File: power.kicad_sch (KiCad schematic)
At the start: 28 parts, among them U5 TPS54302, U6 TPS54302

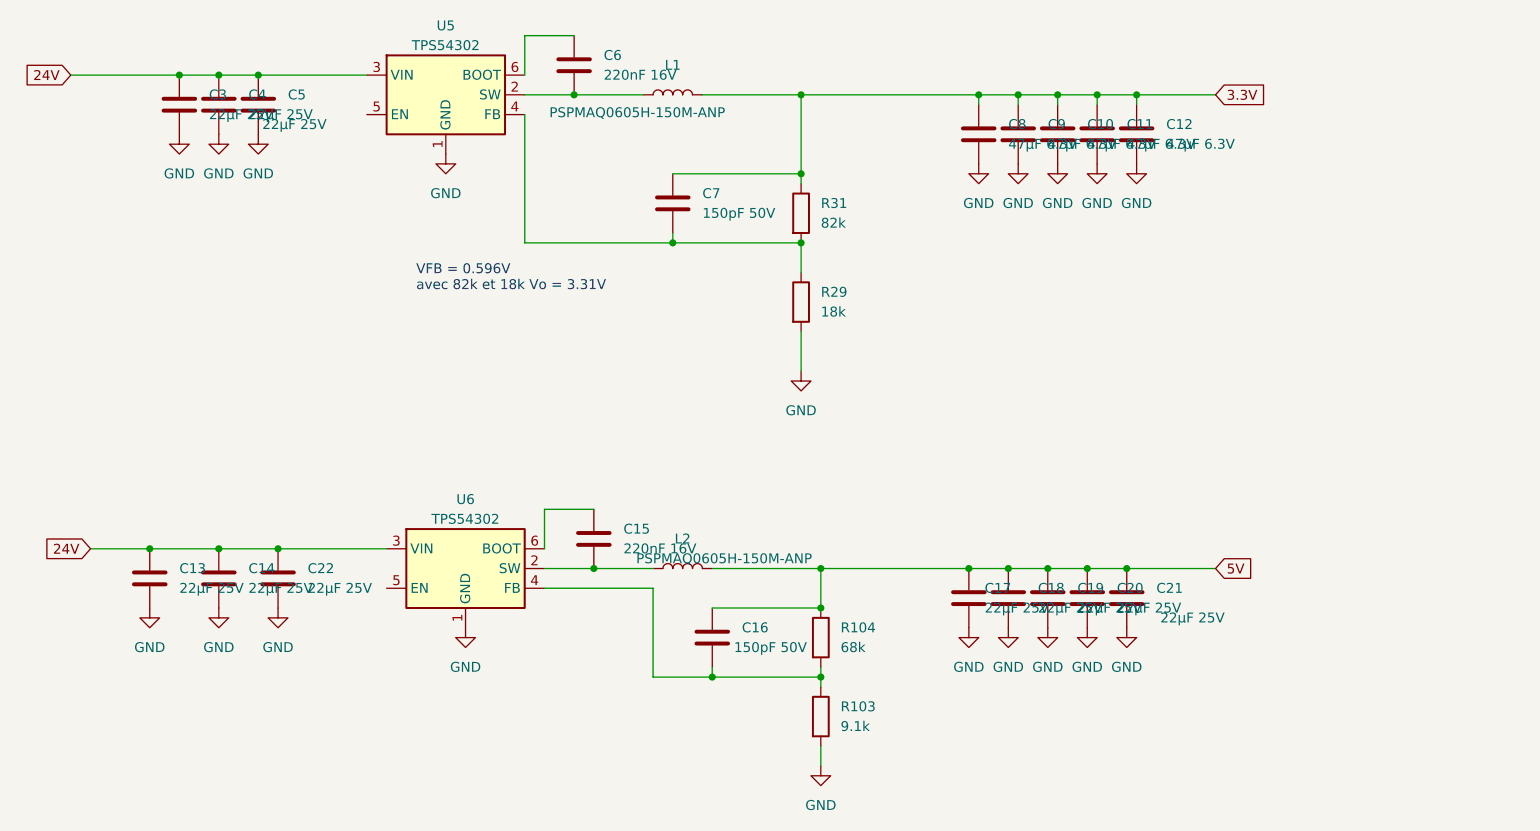
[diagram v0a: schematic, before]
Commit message: update schematic
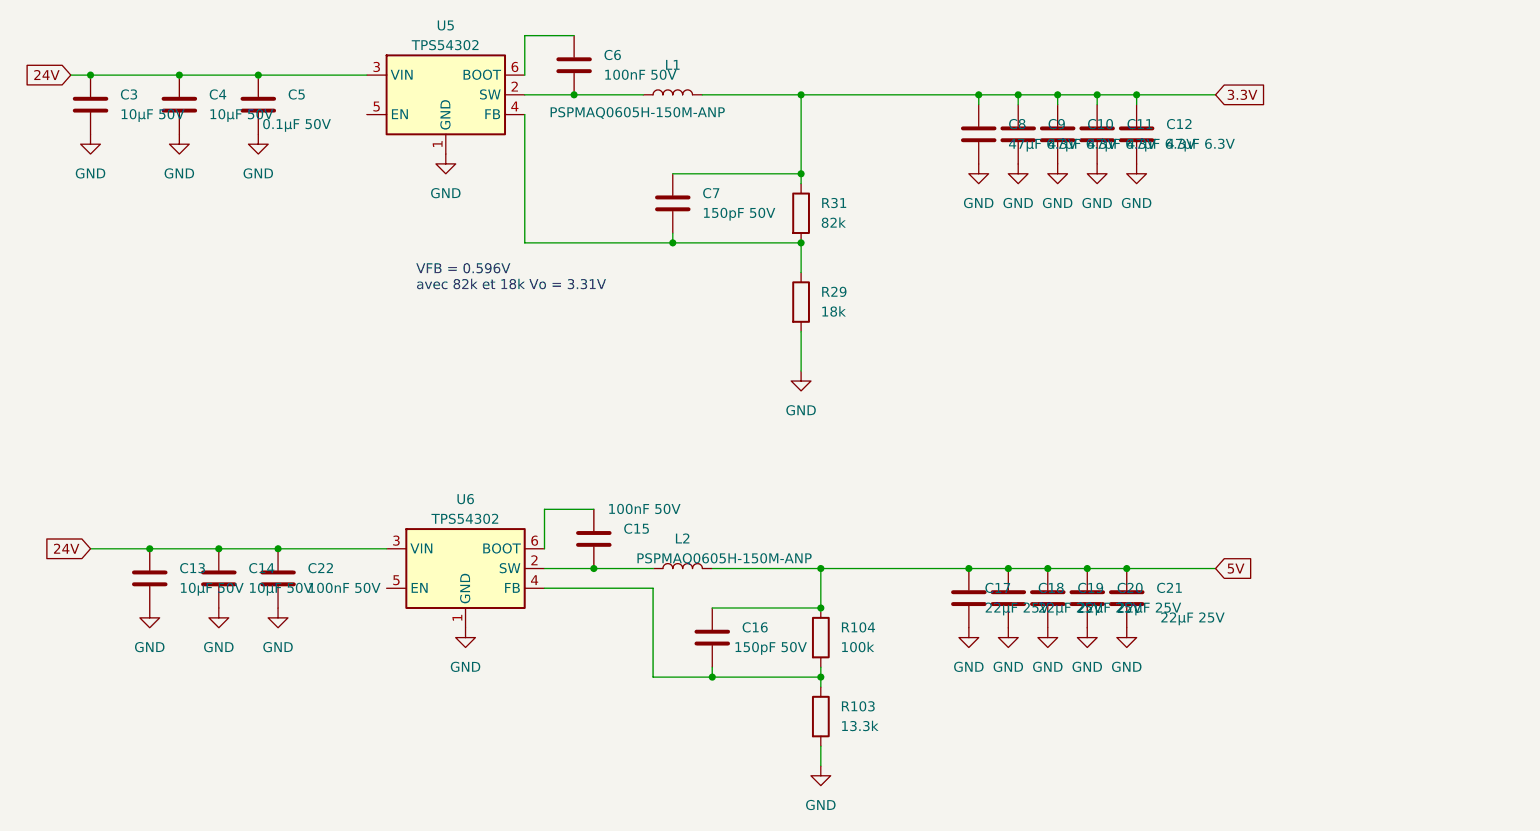
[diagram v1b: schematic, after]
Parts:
- C13, C14, C3, C4: value 22µF 25V -> 10µF 50V
- C15, C6: value 220nF 16V -> 100nF 50V
- C22: value 22µF 25V -> 100nF 50V
- C5: value 22µF 25V -> 0.1µF 50V
- R103: value 9.1k -> 13.3k
- R104: value 68k -> 100k
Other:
- moved on the sheet: C3, C4
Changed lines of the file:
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@@
 	)
 	(junction
+		(at 49.53 27.94)
+		(diameter 0)
+		(color 0 0 0 0)
+	)
+	(junction
 		(at 132.08 105.41)
 		(diameter 0)
@@
 	)
 	(junction
-		(at 54.61 27.94)
-		(diameter 0)
-		(color 0 0 0 0)
-	)
-	(junction
-		(at 49.53 27.94)
+		(at 161.29 91.44)
 		(diameter 0)
 		(color 0 0 0 0)
 	)
 	(junction
-		(at 161.29 91.44)
+		(at 38.1 27.94)
 		(diameter 0)
 		(color 0 0 0 0)
@@
 	(wire
 		(pts
-			(xy 35.56 27.94) (xy 49.53 27.94)
+			(xy 35.56 27.94) (xy 38.1 27.94)
 		)
 		(stroke
@@
 	(wire
 		(pts
-			(xy 49.53 27.94) (xy 54.61 27.94)
+			(xy 54.61 88.9) (xy 62.23 88.9)
 		)
 		(stroke
@@
 	(wire
 		(pts
-			(xy 54.61 88.9) (xy 62.23 88.9)
+			(xy 109.22 30.48) (xy 100.33 30.48)
 		)
 		(stroke
@@
 	(wire
 		(pts
-			(xy 109.22 30.48) (xy 100.33 30.48)
+			(xy 132.08 105.41) (xy 132.08 106.68)
 		)
 		(stroke
@@
 	(wire
 		(pts
-			(xy 132.08 105.41) (xy 132.08 106.68)
+			(xy 38.1 27.94) (xy 49.53 27.94)
 		)
 		(stroke
@@
 	(wire
 		(pts
-			(xy 54.61 27.94) (xy 59.69 27.94)
+			(xy 93.98 27.94) (xy 93.98 22.86)
 		)
 		(stroke
@@
 	(wire
 		(pts
-			(xy 93.98 27.94) (xy 93.98 22.86)
+			(xy 49.53 27.94) (xy 59.69 27.94)
 		)
 		(stroke
@@
 			)
 		)
-		(property "Value" "22µF 25V"
+		(property "Value" "10µF 50V"
 			(at 58.42 93.98 0)
 			(effects
@@
 	(symbol
 		(lib_id "Device:C")
-		(at 49.53 31.75 0)
+		(at 38.1 31.75 0)
 		(unit 1)
 		(exclude_from_sim no)
@@
 		(dnp no)
 		(property "Reference" "C3"
-			(at 53.34 30.48 0)
+			(at 41.91 30.48 0)
 			(effects
 				(font
@@
 			)
 		)
-		(property "Value" "22µF 25V"
-			(at 53.34 33.02 0)
+		(property "Value" "10µF 50V"
+			(at 41.91 33.02 0)
 			(effects
 				(font
@@
 		)
 		(property "Footprint" "Capacitor_SMD:C_0805_2012Metric"
-			(at 50.4952 35.56 0)
+			(at 39.0652 35.56 0)
 			(effects
 				(font
@@
 		)
 		(property "Datasheet" "~"
-			(at 49.53 31.75 0)
+			(at 38.1 31.75 0)
 			(effects
 				(font
@@
 		)
 		(property "Description" ""
-			(at 49.53 31.75 0)
+			(at 38.1 31.75 0)
 			(effects
 				(font
@@
 	(symbol
 		(lib_id "power:GND")
-		(at 49.53 35.56 0)
+		(at 38.1 35.56 0)
 		(unit 1)
 		(exclude_from_sim no)
@@
 		(fields_autoplaced yes)
 		(property "Reference" "#PWR023"
-			(at 49.53 41.91 0)
+			(at 38.1 41.91 0)
 			(effects
 				(font
@@
 		)
 		(property "Value" "GND"
-			(at 49.53 40.64 0)
+			(at 38.1 40.64 0)
 			(effects
 				(font
@@
 		)
 		(property "Footprint" ""
-			(at 49.53 35.56 0)
+			(at 38.1 35.56 0)
 			(effects
 				(font
@@
 		)
 		(property "Datasheet" ""
-			(at 49.53 35.56 0)
+			(at 38.1 35.56 0)
 			(effects
 				(font
@@
 		)
 		(property "Description" ""
-			(at 49.53 35.56 0)
+			(at 38.1 35.56 0)
 			(effects
 				(font
@@
 		(on_board yes)
 		(dnp no)
-		(fields_autoplaced yes)
 		(property "Reference" "C15"
 			(at 106.68 86.36 0)
@@
 			)
 		)
-		(property "Value" "220nF 16V"
-			(at 106.68 88.9 0)
+		(property "Value" "100nF 50V"
+			(at 104.648 83.82 0)
 			(effects
 				(font
@@
 			)
 		)
-		(property "Value" "22µF 25V"
+		(property "Value" "100nF 50V"
 			(at 66.04 93.98 0)
 			(effects
@@
 			)
 		)
-		(property "Value" "68k"
+		(property "Value" "100k"
 			(at 134.62 101.5999 0)
 			(effects
@@
 		(fields_autoplaced yes)
 		(property "Reference" "R103"
-			(at 134.62 109.22 0)
+			(at 134.62 109.2199 0)
 			(effects
 				(font
@@
 			)
 		)
-		(property "Value" "9.1k"
-			(at 134.62 111.76 0)
+		(property "Value" "13.3k"
+			(at 134.62 111.7599 0)
 			(effects
 				(font
@@
 	(symbol
 		(lib_id "power:GND")
-		(at 54.61 35.56 0)
+		(at 49.53 35.56 0)
 		(unit 1)
 		(exclude_from_sim no)
@@
 		(fields_autoplaced yes)
 		(property "Reference" "#PWR025"
-			(at 54.61 41.91 0)
+			(at 49.53 41.91 0)
 			(effects
 				(font
@@
 		)
 		(property "Value" "GND"
-			(at 54.61 40.64 0)
+			(at 49.53 40.64 0)
 			(effects
 				(font
@@
 		)
 		(property "Footprint" ""
-			(at 54.61 35.56 0)
+			(at 49.53 35.56 0)
 			(effects
 				(font
@@
 		)
 		(property "Datasheet" ""
-			(at 54.61 35.56 0)
+			(at 49.53 35.56 0)
 			(effects
 				(font
@@
 		)
 		(property "Description" ""
-			(at 54.61 35.56 0)
+			(at 49.53 35.56 0)
 			(effects
 				(font
@@
 		(fields_autoplaced yes)
 		(property "Reference" "C6"
-			(at 104.14 25.4 0)
+			(at 104.14 25.3999 0)
 			(effects
 				(font
@@
 			)
 		)
-		(property "Value" "220nF 16V"
-			(at 104.14 27.94 0)
+		(property "Value" "100nF 50V"
+			(at 104.14 27.9399 0)
 			(effects
 				(font
@@
 			)
 		)
-		(property "Value" "22µF 25V"
+		(property "Value" "10µF 50V"
 			(at 49.53 93.98 0)
 			(effects
@@
 			)
 		)
-		(property "Value" "22µF 25V"
+		(property "Value" "0.1µF 50V"
 			(at 60.198 34.29 0)
 			(effects
@@
 	(symbol
 		(lib_id "Device:C")
-		(at 54.61 31.75 0)
+		(at 49.53 31.75 0)
 		(unit 1)
 		(exclude_from_sim no)
@@
 		(dnp no)
 		(property "Reference" "C4"
-			(at 58.42 30.48 0)
+			(at 53.34 30.48 0)
 			(effects
 				(font
@@
 			)
 		)
-		(property "Value" "22µF 25V"
-			(at 58.42 33.02 0)
+		(property "Value" "10µF 50V"
+			(at 53.34 33.02 0)
 			(effects
 				(font
@@
 		)
 		(property "Footprint" "Capacitor_SMD:C_0805_2012Metric"
-			(at 55.5752 35.56 0)
+			(at 50.4952 35.56 0)
 			(effects
 				(font
@@
 		)
 		(property "Datasheet" "~"
-			(at 54.61 31.75 0)
+			(at 49.53 31.75 0)
 			(effects
 				(font
@@
 		)
 		(property "Description" ""
-			(at 54.61 31.75 0)
+			(at 49.53 31.75 0)
 			(effects
 				(font

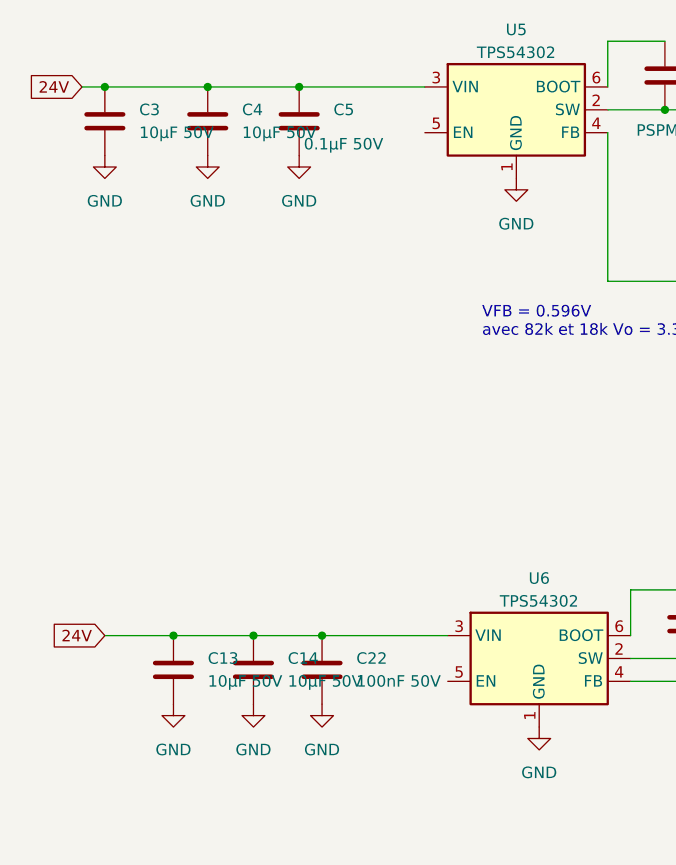
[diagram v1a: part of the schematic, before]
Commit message: update capa footprint
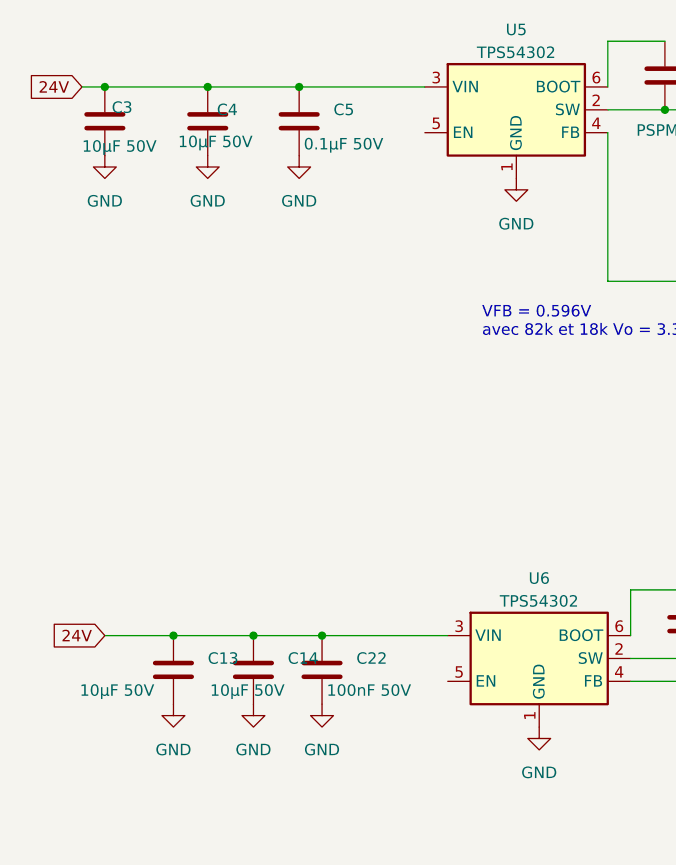
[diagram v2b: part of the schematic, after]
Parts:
- C13, C14, C22, C3, C4: footprint Capacitor_SMD:C_0805_2012Metric -> Capacitor_SMD:C_1206_3216Metric
- C15: footprint Capacitor_SMD:C_0402_1005Metric -> Capacitor_SMD:C_1206_3216Metric
- C16: footprint Capacitor_SMD:C_0603_1608Metric -> Capacitor_SMD:C_1206_3216Metric
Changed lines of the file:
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@@
 		)
 		(property "Value" "10µF 50V"
-			(at 58.42 93.98 0)
-			(effects
-				(font
-					(size 1.27 1.27)
-				)
-				(justify left)
-			)
-		)
-		(property "Footprint" "Capacitor_SMD:C_0805_2012Metric"
+			(at 49.784 94.996 0)
+			(effects
+				(font
+					(size 1.27 1.27)
+				)
+				(justify left)
+			)
+		)
+		(property "Footprint" "Capacitor_SMD:C_1206_3216Metric"
 			(at 55.5752 96.52 0)
 			(effects
@@
 		(dnp no)
 		(property "Reference" "C3"
-			(at 41.91 30.48 0)
+			(at 38.862 30.226 0)
 			(effects
 				(font
@@
 		)
 		(property "Value" "10µF 50V"
-			(at 41.91 33.02 0)
-			(effects
-				(font
-					(size 1.27 1.27)
-				)
-				(justify left)
-			)
-		)
-		(property "Footprint" "Capacitor_SMD:C_0805_2012Metric"
+			(at 35.56 34.544 0)
+			(effects
+				(font
+					(size 1.27 1.27)
+				)
+				(justify left)
+			)
+		)
+		(property "Footprint" "Capacitor_SMD:C_1206_3216Metric"
 			(at 39.0652 35.56 0)
 			(effects
@@
 			)
 		)
-		(property "Footprint" "Capacitor_SMD:C_0402_1005Metric"
+		(property "Footprint" "Capacitor_SMD:C_1206_3216Metric"
 			(at 103.8352 91.44 0)
 			(effects
@@
 		)
 		(property "Value" "100nF 50V"
-			(at 66.04 93.98 0)
-			(effects
-				(font
-					(size 1.27 1.27)
-				)
-				(justify left)
-			)
-		)
-		(property "Footprint" "Capacitor_SMD:C_0805_2012Metric"
+			(at 62.738 94.996 0)
+			(effects
+				(font
+					(size 1.27 1.27)
+				)
+				(justify left)
+			)
+		)
+		(property "Footprint" "Capacitor_SMD:C_1206_3216Metric"
 			(at 63.1952 96.52 0)
 			(effects
@@
 		)
 		(property "Value" "10µF 50V"
-			(at 49.53 93.98 0)
-			(effects
-				(font
-					(size 1.27 1.27)
-				)
-				(justify left)
-			)
-		)
-		(property "Footprint" "Capacitor_SMD:C_0805_2012Metric"
+			(at 35.306 94.996 0)
+			(effects
+				(font
+					(size 1.27 1.27)
+				)
+				(justify left)
+			)
+		)
+		(property "Footprint" "Capacitor_SMD:C_1206_3216Metric"
 			(at 46.6852 96.52 0)
 			(effects
@@
 		(dnp no)
 		(property "Reference" "C4"
-			(at 53.34 30.48 0)
+			(at 50.546 30.48 0)
 			(effects
 				(font
@@
 		)
 		(property "Value" "10µF 50V"
-			(at 53.34 33.02 0)
-			(effects
-				(font
-					(size 1.27 1.27)
-				)
-				(justify left)
-			)
-		)
-		(property "Footprint" "Capacitor_SMD:C_0805_2012Metric"
+			(at 46.228 34.036 0)
+			(effects
+				(font
+					(size 1.27 1.27)
+				)
+				(justify left)
+			)
+		)
+		(property "Footprint" "Capacitor_SMD:C_1206_3216Metric"
 			(at 50.4952 35.56 0)
 			(effects
@@
 			)
 		)
-		(property "Footprint" "Capacitor_SMD:C_0603_1608Metric"
+		(property "Footprint" "Capacitor_SMD:C_1206_3216Metric"
 			(at 119.0752 104.14 0)
 			(effects

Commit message: test nouvelle forme de carte
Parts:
- C15: footprint Capacitor_SMD:C_1206_3216Metric -> Capacitor_SMD:C_0402_1005Metric
- C22: footprint Capacitor_SMD:C_1206_3216Metric -> Capacitor_SMD:C_0805_2012Metric
- C7: footprint Capacitor_SMD:C_0603_1608Metric -> Capacitor_SMD:C_1206_3216Metric
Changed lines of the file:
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@@
 			)
 		)
-		(property "Footprint" "Capacitor_SMD:C_0603_1608Metric"
+		(property "Footprint" "Capacitor_SMD:C_1206_3216Metric"
 			(at 113.9952 48.26 0)
 			(effects
@@
 			)
 		)
-		(property "Footprint" "Capacitor_SMD:C_1206_3216Metric"
+		(property "Footprint" "Capacitor_SMD:C_0402_1005Metric"
 			(at 103.8352 91.44 0)
 			(effects
@@
 			)
 		)
-		(property "Footprint" "Capacitor_SMD:C_1206_3216Metric"
+		(property "Footprint" "Capacitor_SMD:C_0805_2012Metric"
 			(at 63.1952 96.52 0)
 			(effects

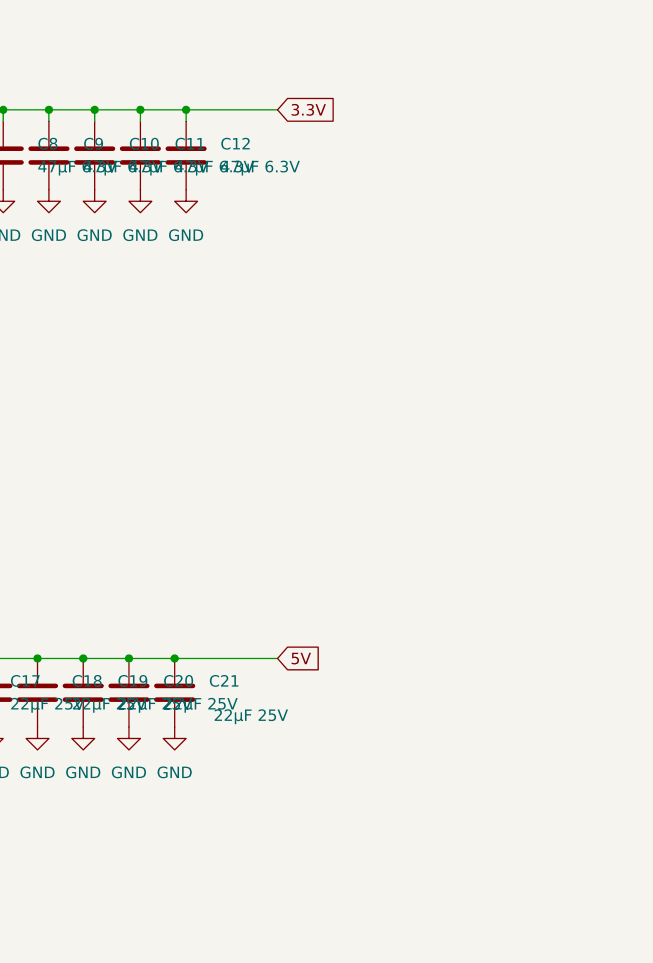
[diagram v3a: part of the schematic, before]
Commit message: add connectors on alim
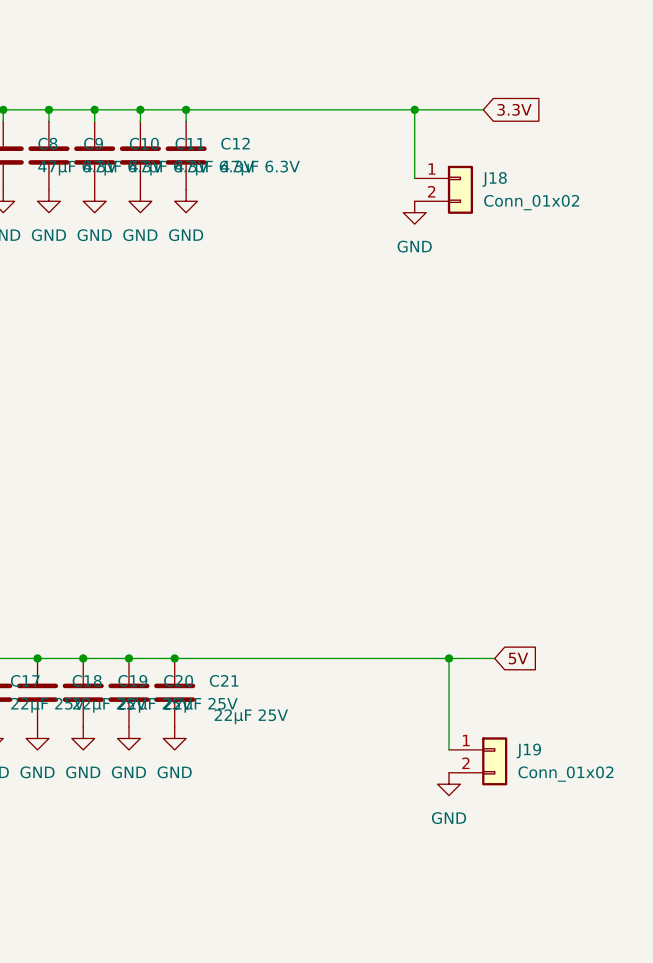
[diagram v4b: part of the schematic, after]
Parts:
- added J18, J19: Conn_01x02, Connector_PinHeader_2.54mm:PinHeader_1x02_P2.54mm_Vertical, symbol Connector_Generic:Conn_01x02
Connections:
- net 3.3V: now also J18.1 (Pin_1)
- net 5V: now also J19.1 (Pin_1)
- net GND: now also J18.2 (Pin_2), J19.2 (Pin_2)

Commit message: update
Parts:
- J18, J19: now left out of the parts list
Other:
- moved on the sheet: L1
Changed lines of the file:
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@@
 	(wire
 		(pts
-			(xy 116.84 30.48) (xy 129.54 30.48)
+			(xy 118.11 30.48) (xy 129.54 30.48)
 		)
 		(stroke
@@
 	(wire
 		(pts
-			(xy 109.22 30.48) (xy 100.33 30.48)
+			(xy 110.49 30.48) (xy 100.33 30.48)
 		)
 		(stroke
@@
 		(unit 1)
 		(exclude_from_sim no)
-		(in_bom yes)
+		(in_bom no)
 		(on_board yes)
 		(dnp no)
@@
 		(on_board yes)
 		(dnp no)
-		(fields_autoplaced yes)
 		(property "Reference" "C6"
 			(at 104.14 25.3999 0)
@@
 		)
 		(property "Value" "100nF 50V"
-			(at 104.14 27.9399 0)
+			(at 98.298 23.368 0)
 			(effects
 				(font
@@
 	(symbol
 		(lib_id "Device:L")
-		(at 113.03 30.48 90)
+		(at 114.3 30.48 90)
 		(unit 1)
 		(exclude_from_sim no)
@@
 		(dnp no)
 		(property "Reference" "L1"
-			(at 113.03 26.67 90)
+			(at 114.3 25.908 90)
 			(effects
 				(font
@@
 		)
 		(property "Value" "PSPMAQ0605H-150M-ANP"
-			(at 108.458 32.766 90)
+			(at 109.728 32.766 90)
 			(effects
 				(font
@@
 		)
 		(property "Footprint" "7Robot_lib:Prod_Tech_7.1x6.6mm"
-			(at 113.03 30.48 0)
+			(at 114.3 30.48 0)
 			(effects
 				(font
@@
 		)
 		(property "Datasheet" "~"
-			(at 113.03 30.48 0)
+			(at 114.3 30.48 0)
 			(effects
 				(font
@@
 		)
 		(property "Description" ""
-			(at 113.03 30.48 0)
+			(at 114.3 30.48 0)
 			(effects
 				(font
@@
 		(unit 1)
 		(exclude_from_sim no)
-		(in_bom yes)
+		(in_bom no)
 		(on_board yes)
 		(dnp no)
